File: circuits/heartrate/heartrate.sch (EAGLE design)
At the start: 21 parts

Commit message: Created pulse sensor layout
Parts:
- !ENABLE, GND, OUT, VDD: value MOUNT-PAD-ROUND2.8 -> LSP10; device holes:MOUNT-PAD-ROUND2.8 -> solpad:LSP10
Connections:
- net GND-ISO: now also GND.MP; no longer GND.MOUNT
- net N$2: now also VDD.MP; no longer VDD.MOUNT
- net N$3: now also !ENABLE.MP; no longer !ENABLE.MOUNT
- net OUT: now also OUT.MP; no longer OUT.MOUNT
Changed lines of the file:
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@@
 <part name="R7" library="SparkFun-Passives" deviceset="RESISTOR" device="0603-RES" value="3.3M"/>
 <part name="U$4" library="MedStatCustom" deviceset="MCP6001" device=""/>
-<part name="OUT" library="holes" deviceset="MOUNT-PAD-ROUND" device="2.8"/>
-<part name="!ENABLE" library="holes" deviceset="MOUNT-PAD-ROUND" device="2.8"/>
-<part name="VDD" library="holes" deviceset="MOUNT-PAD-ROUND" device="2.8"/>
-<part name="GND" library="holes" deviceset="MOUNT-PAD-ROUND" device="2.8"/>
 <part name="GND-ISO1" library="SparkFun-Aesthetics" deviceset="GND-ISO" device=""/>
 <part name="U$5" library="GeekAmmo" deviceset="P-CHANNEL-MOSFET" device=""/>
+<part name="!ENABLE" library="solpad" deviceset="LSP10" device=""/>
+<part name="VDD" library="solpad" deviceset="LSP10" device=""/>
+<part name="OUT" library="solpad" deviceset="LSP10" device=""/>
+<part name="GND" library="solpad" deviceset="LSP10" device=""/>
 </parts>
 <sheets>
@@
 <instance part="R7" gate="G$1" x="177.8" y="68.58" rot="R180"/>
 <instance part="U$4" gate="G$1" x="180.34" y="50.8"/>
-<instance part="OUT" gate="G$1" x="208.28" y="50.8"/>
-<instance part="!ENABLE" gate="G$1" x="208.28" y="86.36"/>
-<instance part="VDD" gate="G$1" x="208.28" y="76.2"/>
-<instance part="GND" gate="G$1" x="208.28" y="30.48"/>
 <instance part="GND-ISO1" gate="G$1" x="132.08" y="27.94"/>
 <instance part="U$5" gate="G$1" x="193.04" y="78.74" rot="R270"/>
+<instance part="!ENABLE" gate="1" x="208.28" y="86.36" rot="R270"/>
+<instance part="VDD" gate="1" x="208.28" y="76.2" rot="R270"/>
+<instance part="OUT" gate="1" x="208.28" y="50.8" rot="R270"/>
+<instance part="GND" gate="1" x="208.28" y="30.48" rot="R270"/>
 </instances>
 <busses>
@@
 <pinref part="U$4" gate="G$1" pin="VOUT"/>
 <wire x1="185.42" y1="50.8" x2="187.96" y2="50.8" width="0.2032" layer="91"/>
-<pinref part="OUT" gate="G$1" pin="MOUNT"/>
 <wire x1="187.96" y1="50.8" x2="205.74" y2="50.8" width="0.2032" layer="91"/>
 <label x="187.96" y="48.26" size="1.778" layer="95"/>
+<pinref part="OUT" gate="1" pin="MP"/>
 </segment>
 </net>
@@
 <wire x1="177.8" y1="43.942" x2="177.8" y2="30.48" width="0.2032" layer="91"/>
 <wire x1="177.8" y1="30.48" x2="162.56" y2="30.48" width="0.2032" layer="91"/>
-<pinref part="GND" gate="G$1" pin="MOUNT"/>
 <wire x1="177.8" y1="30.48" x2="205.74" y2="30.48" width="0.2032" layer="91"/>
 <pinref part="GND-ISO1" gate="G$1" pin="GND-ISO"/>
 <junction x="132.08" y="30.48"/>
+<pinref part="GND" gate="1" pin="MP"/>
 </segment>
 </net>
@@
 <segment>
 <pinref part="U$5" gate="G$1" pin="S"/>
-<pinref part="VDD" gate="G$1" pin="MOUNT"/>
 <wire x1="200.66" y1="76.2" x2="205.74" y2="76.2" width="0.2032" layer="91"/>
+<pinref part="VDD" gate="1" pin="MP"/>
 </segment>
 </net>
@@
 <pinref part="U$5" gate="G$1" pin="G"/>
 <wire x1="195.58" y1="83.82" x2="195.58" y2="86.36" width="0.2032" layer="91"/>
-<pinref part="!ENABLE" gate="G$1" pin="MOUNT"/>
 <wire x1="195.58" y1="86.36" x2="205.74" y2="86.36" width="0.2032" layer="91"/>
+<pinref part="!ENABLE" gate="1" pin="MP"/>
 </segment>
 </net>

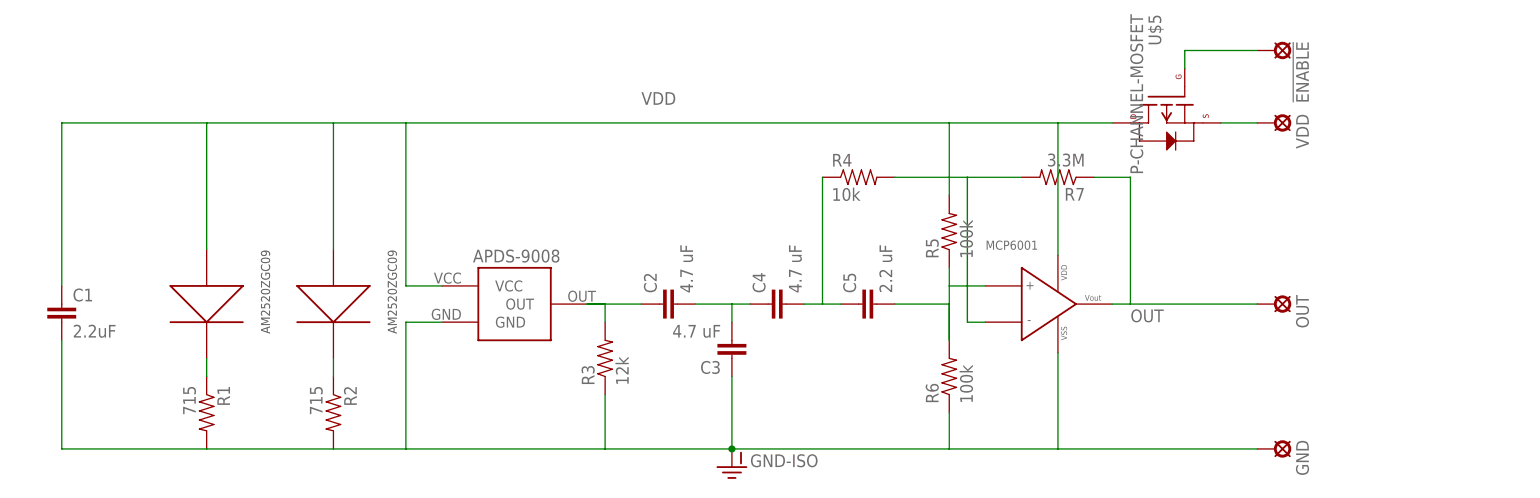
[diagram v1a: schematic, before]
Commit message: changed resistor and capacitor sizes
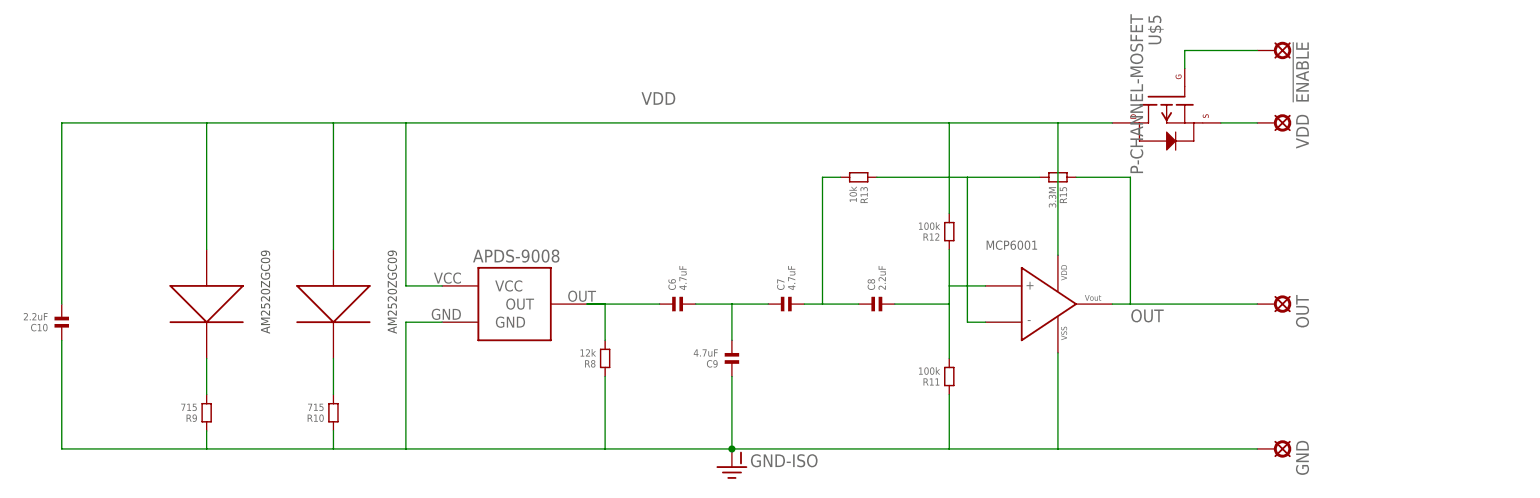
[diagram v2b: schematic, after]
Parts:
- removed C1: 2.2uF, SparkFun-Passives:CAP0603-CAP
- removed C2, C3, C4: 4.7 uF, SparkFun-Capacitors:CAP0603-CAP
- removed C5: 2.2 uF, SparkFun-Capacitors:CAP0603-CAP
- removed R1, R2: 715, SparkFun-Passives:RESISTOR0603-RES
- removed R3: 12k, SparkFun-Passives:RESISTOR0603-RES
- removed R4: 10k, SparkFun-Passives:RESISTOR0603-RES
- removed R5, R6: 100k, SparkFun-Passives:RESISTOR0603-RES
- removed R7: 3.3M, SparkFun-Passives:RESISTOR0603-RES
- added C10, C8: 2.2uF, standardparts:CAPACITOR.0201
- added C6, C7, C9: 4.7uF, standardparts:CAPACITOR.0201
- added R10, R9: 715, standardparts:RESISTOR.0201
- added R11, R12: 100k, standardparts:RESISTOR.0201
- added R13: 10k, standardparts:RESISTOR.0201
- added R15: 3.3M, standardparts:RESISTOR.0201
- added R8: 12k, standardparts:RESISTOR.0201
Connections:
- net GND-ISO: now also C10.1, C9.1, R10.1, R11.1, R8.1, R9.1; no longer C1.2, C3.1, R1.2, R2.2, R3.1, R6.1
- net N$1: now also R9.2; no longer R1.1
- net N$10: now also C8.2, R11.2, R12.1; no longer C5.2, R5.1, R6.2
- net N$12: now also R13.1, R15.2; no longer R4.2, R7.2
- net N$4: now also R10.2; no longer R2.1
- net N$5: now also C6.1, R8.2; no longer C2.1, R3.2
- net N$6: now also C6.2, C7.1, C9.2; no longer C2.2, C3.2, C4.1
- net N$7: now also C7.2, C8.1, R13.2; no longer C4.2, C5.1, R4.1
- net OUT: now also R15.1; no longer R7.1
- net VDD: now also C10.2, R12.2; no longer C1.1, R5.2

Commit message: finished new heart rate sensor layout
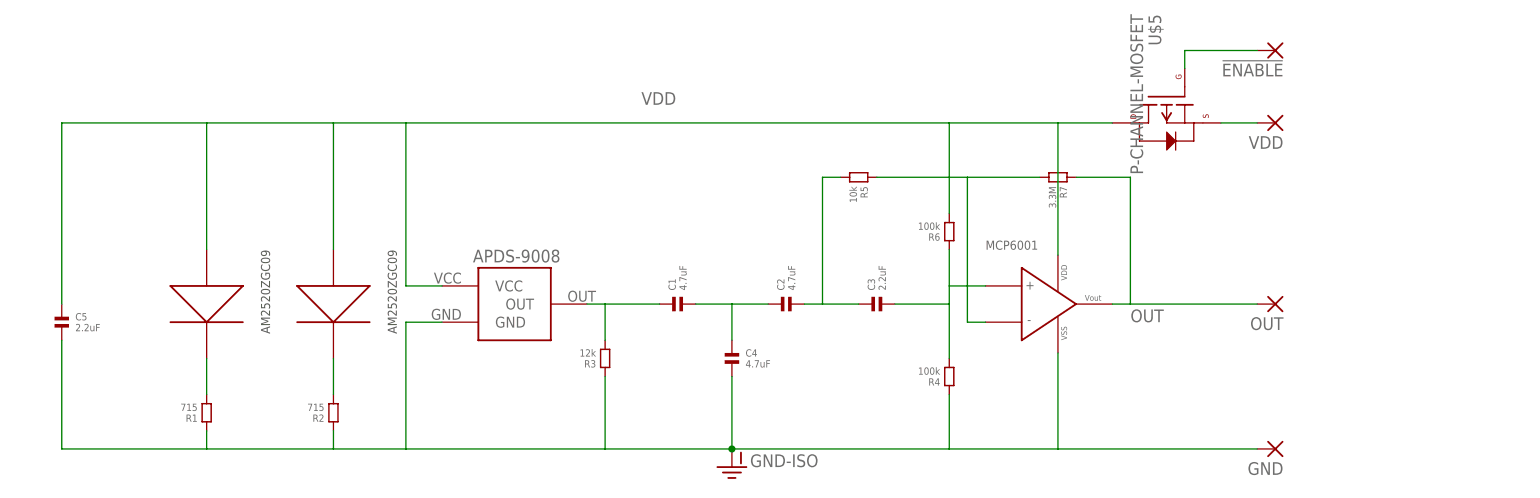
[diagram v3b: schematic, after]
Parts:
- removed C10, C8: 2.2uF, standardparts:CAPACITOR.0201
- removed C6, C7, C9: 4.7uF, standardparts:CAPACITOR.0201
- removed R10, R9: 715, standardparts:RESISTOR.0201
- removed R11, R12: 100k, standardparts:RESISTOR.0201
- removed R13: 10k, standardparts:RESISTOR.0201
- removed R15: 3.3M, standardparts:RESISTOR.0201
- removed R8: 12k, standardparts:RESISTOR.0201
- added C1, C2, C4: 4.7uF, standardparts:CAPACITOR.0402
- added C3, C5: 2.2uF, standardparts:CAPACITOR.0402
- added R1, R2: 715, standardparts:RESISTOR.0402
- added R3: 12k, standardparts:RESISTOR.0402
- added R4, R6: 100k, standardparts:RESISTOR.0402
- added R5: 10k, standardparts:RESISTOR.0402
- added R7: 3.3M, standardparts:RESISTOR.0402
- !ENABLE, GND, OUT, VDD: value LSP10 -> (none); device solpad:LSP10 -> wirepad:SMD2
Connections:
- removed net GND-ISO: C10.1, C9.1, GND.MP, R10.1, R11.1, R8.1, R9.1, U$3.GND, U$4.VSS
- new net GND: C4.2, C5.2, GND.P, R1.1, R2.1, R3.1, R4.1, U$3.GND, U$4.VSS
- net N$1: now also R1.2; no longer R9.2
- net N$10: now also C3.2, R4.2, R6.1; no longer C8.2, R11.2, R12.1
- net N$12: now also R5.1, R7.2; no longer R13.1, R15.2
- net N$2: now also VDD.P; no longer VDD.MP
- net N$3: now also !ENABLE.P; no longer !ENABLE.MP
- net N$4: now also R2.2; no longer R10.2
- net N$5: now also C1.1, R3.2; no longer C6.1, R8.2
- net N$6: now also C1.2, C2.1, C4.1; no longer C6.2, C7.1, C9.2
- net N$7: now also C2.2, C3.1, R5.2; no longer C7.2, C8.1, R13.2
- net OUT: now also OUT.P, R7.1; no longer OUT.MP, R15.1
- net VDD: now also C5.1, R6.2; no longer C10.2, R12.2
